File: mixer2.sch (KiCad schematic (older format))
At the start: 24 parts, among them Q1 MMBT5089, U2 SA612, Y1 Crystal

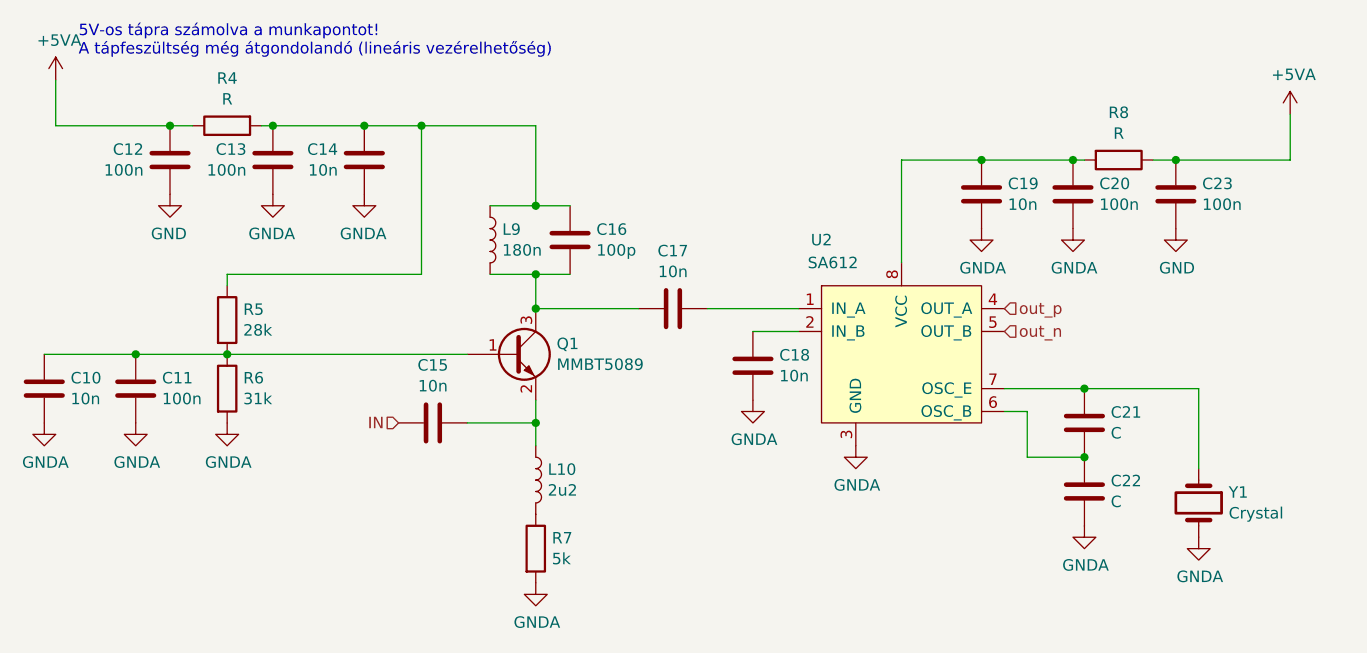
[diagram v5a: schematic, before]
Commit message: Receiver test panel ++
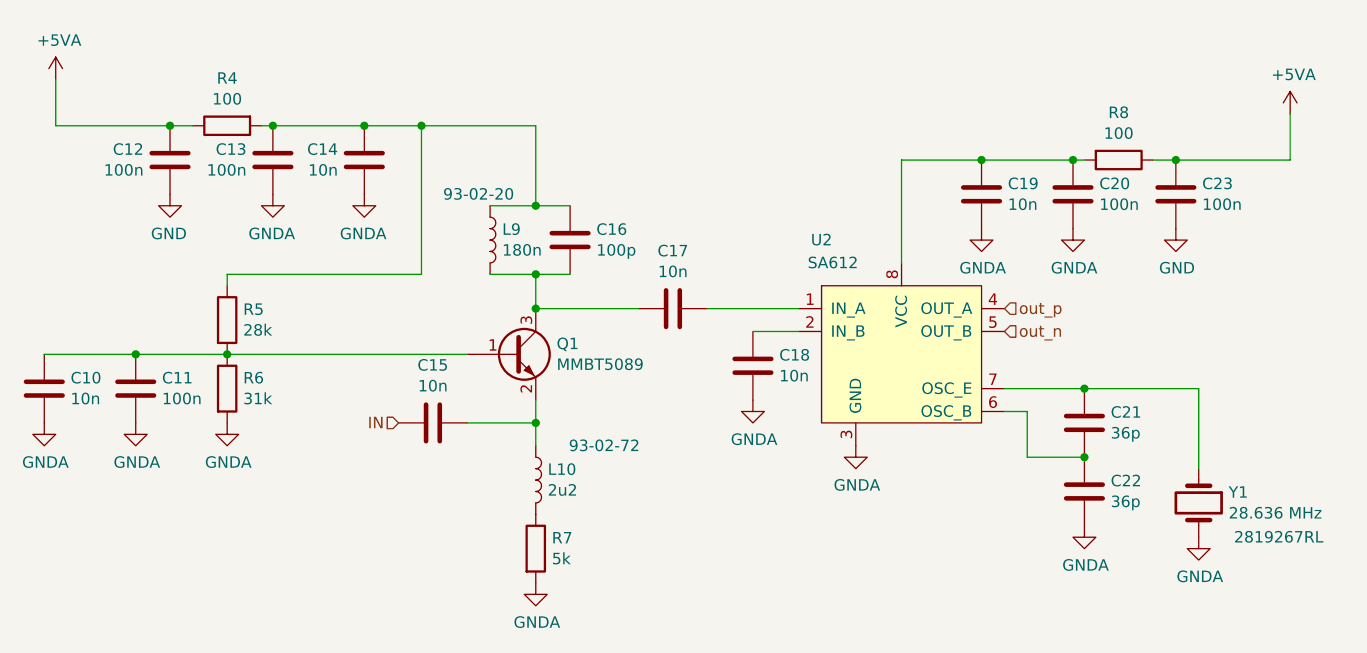
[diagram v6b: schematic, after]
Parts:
- C21, C22: value C -> 36p
- L10: footprint (none) -> Inductor_SMD:L_0805_2012Metric_Pad1.15x1.40mm_HandSolder; Lomex (none) -> 93-02-72
- L9: footprint (none) -> Inductor_SMD:L_1210_3225Metric_Pad1.42x2.65mm_HandSolder; Lomex (none) -> 93-02-20
- R4, R8: value R -> 100
- Y1: value Crystal -> 28.636 MHz; Farnell (none) -> 2819267RL
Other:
- note removed: "5V-os tápra számolva a munkapontot!\nA tápfeszültség még átgondolandó (lineáris vezérelhetőség)"
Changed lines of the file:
@@
 P 7700 3050
 F 0 "R8" V 7493 3050 50  0000 C CNN
-F 1 "R" V 7584 3050 50  0000 C CNN
+F 1 "100" V 7584 3050 50  0000 C CNN
 F 2 "Resistor_SMD:R_0805_2012Metric_Pad1.15x1.40mm_HandSolder" V 7630 3050 50  0001 C CNN
 F 3 "~" H 7700 3050 50  0001 C CNN
@@
 F 0 "L9" H 5003 3446 50  0000 L CNN
 F 1 "180n" H 5003 3355 50  0000 L CNN
-F 2 "" H 4950 3400 50  0001 C CNN
+F 2 "Inductor_SMD:L_1210_3225Metric_Pad1.42x2.65mm_HandSolder" H 4950 3400 50  0001 C CNN
 F 3 "~" H 4950 3400 50  0001 C CNN
+F 4 "93-02-20" H 4900 3600 50  0000 C CNN "Lomex"
 	1    4950 3400
 	1    0    0    -1
@@
 F 0 "L10" H 5202 4496 50  0000 L CNN
 F 1 "2u2" H 5202 4405 50  0000 L CNN
-F 2 "" H 5150 4450 50  0001 C CNN
+F 2 "Inductor_SMD:L_0805_2012Metric_Pad1.15x1.40mm_HandSolder" H 5150 4450 50  0001 C CNN
 F 3 "~" H 5150 4450 50  0001 C CNN
+F 4 "93-02-72 " H 5450 4600 50  0000 C CNN "Lomex"
 	1    5150 4450
 	1    0    0    -1
@@
 P 8050 4550
 F 0 "Y1" V 8004 4681 50  0000 L CNN
-F 1 "Crystal" V 8095 4681 50  0000 L CNN
+F 1 "28.636 MHz" V 8095 4681 50  0000 L CNN
 F 2 "Crystal:Crystal_HC49-U_Vertical" H 8050 4550 50  0001 C CNN
 F 3 "~" H 8050 4550 50  0001 C CNN
+F 4 "2819267RL" V 8200 4900 50  0000 C CNN "Farnell"
 	1    8050 4550
 	0    1    1    0
@@
 P 7550 4200
 F 0 "C21" H 7665 4246 50  0000 L CNN
-F 1 "C" H 7665 4155 50  0000 L CNN
+F 1 "36p" H 7665 4155 50  0000 L CNN
 F 2 "Capacitor_SMD:C_0805_2012Metric_Pad1.15x1.40mm_HandSolder" H 7588 4050 50  0001 C CNN
 F 3 "~" H 7550 4200 50  0001 C CNN
@@
 P 7550 4500
 F 0 "C22" H 7665 4546 50  0000 L CNN
-F 1 "C" H 7665 4455 50  0000 L CNN
+F 1 "36p" H 7665 4455 50  0000 L CNN
 F 2 "Capacitor_SMD:C_0805_2012Metric_Pad1.15x1.40mm_HandSolder" H 7588 4350 50  0001 C CNN
 F 3 "~" H 7550 4500 50  0001 C CNN
@@
 P 3800 2900
 F 0 "R4" V 3593 2900 50  0000 C CNN
-F 1 "R" V 3684 2900 50  0000 C CNN
+F 1 "100" V 3684 2900 50  0000 C CNN
 F 2 "Resistor_SMD:R_0805_2012Metric_Pad1.15x1.40mm_HandSolder" V 3730 2900 50  0001 C CNN
 F 3 "~" H 3800 2900 50  0001 C CNN
@@
 Wire Wire Line
 	5150 3250 4950 3250
-Text Notes 3150 2600 0    50   ~ 0
-5V-os tápra számolva a munkapontot!\nA tápfeszültség még átgondolandó (lineáris vezérelhetőség)
 Wire Wire Line
 	3800 3600 3800 3550

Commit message: if2_bpf revised + Schematic cleanup
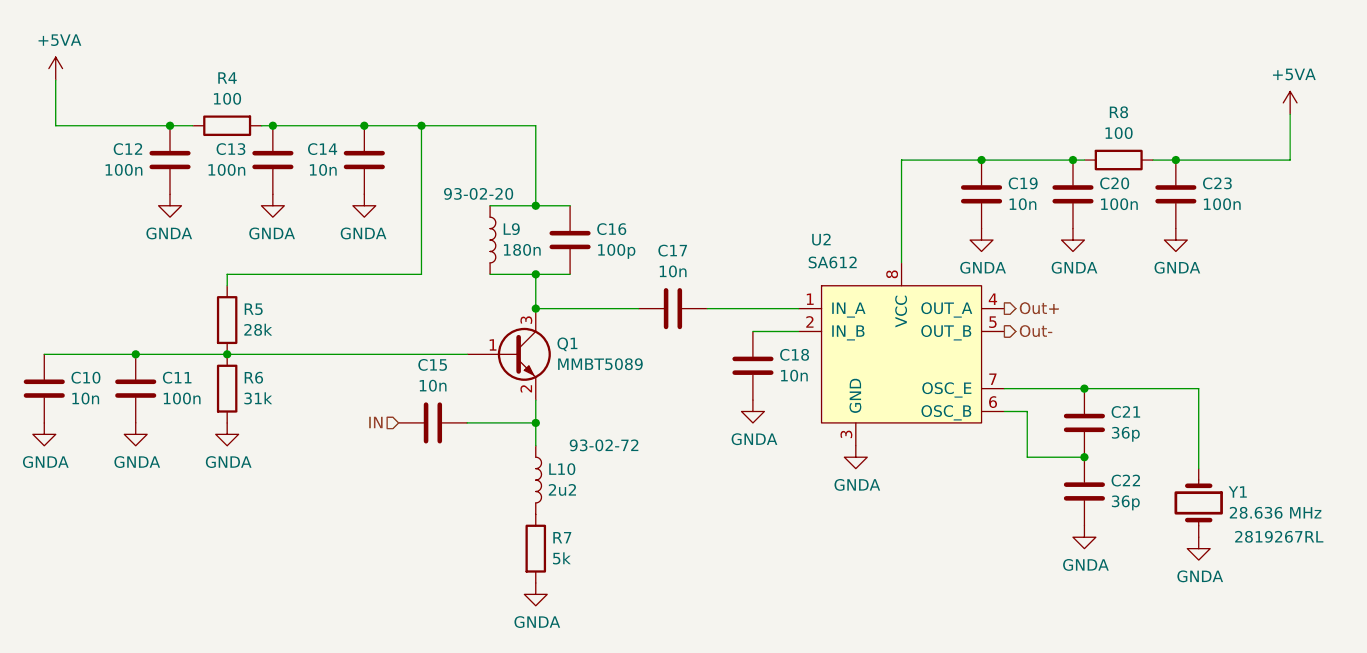
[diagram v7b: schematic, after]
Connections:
- net GND is gone; now on net GNDA: C12.2, C23.2
- net out_n renamed Out-
- net out_p renamed Out+
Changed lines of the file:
@@
-	1    0    0    -1
-$EndComp
-$Comp
-L power:GND #PWR0115
-U 1 1 5FE57211
-P 7950 3350
-F 0 "#PWR0115" H 7950 3100 50  0001 C CNN
-F 1 "GND" H 7955 3177 50  0000 C CNN
-F 2 "" H 7950 3350 50  0001 C CNN
-F 3 "" H 7950 3350 50  0001 C CNN
-	1    7950 3350
 	1    0    0    -1
 $EndComp
@@
 	8450 3050 7950 3050
 Connection ~ 7950 3050
-Text HLabel 7200 3700 2    50   Input ~ 0
-out_p
-Text HLabel 7200 3800 2    50   Input ~ 0
-out_n
+Text HLabel 7200 3700 2    50   Output ~ 0
+Out+
+Text HLabel 7200 3800 2    50   Output ~ 0
+Out-
 $Comp
 L Device:C C18
@@
 	-1   0    0    -1
 $EndComp
-$Comp
-L power:GND #PWR0125
-U 1 1 5FE79CB0
-P 3550 3200
-F 0 "#PWR0125" H 3550 2950 50  0001 C CNN
-F 1 "GND" H 3555 3027 50  0000 C CNN
-F 2 "" H 3550 3200 50  0001 C CNN
-F 3 "" H 3550 3200 50  0001 C CNN
-	1    3550 3200
-	-1   0    0    -1
-$EndComp
 Wire Wire Line
 	3550 2900 3650 2900
@@
 	1    0    0    -1
 $EndComp
+$Comp
+L power:GNDA #PWR?
+U 1 1 6009A572
+P 3550 3200
+F 0 "#PWR?" H 3550 2950 50  0001 C CNN
+F 1 "GNDA" H 3555 3027 50  0000 C CNN
+F 2 "" H 3550 3200 50  0001 C CNN
+F 3 "" H 3550 3200 50  0001 C CNN
+	1    3550 3200
+	-1   0    0    -1
+$EndComp
+$Comp
+L power:GNDA #PWR?
+U 1 1 6009AB1D
+P 7950 3350
+F 0 "#PWR?" H 7950 3100 50  0001 C CNN
+F 1 "GNDA" H 7955 3177 50  0000 C CNN
+F 2 "" H 7950 3350 50  0001 C CNN
+F 3 "" H 7950 3350 50  0001 C CNN
+	1    7950 3350
+	1    0    0    -1
+$EndComp
